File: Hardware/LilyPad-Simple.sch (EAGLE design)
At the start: 43 parts, among them U1 ATMEGA328P_TQFP, U2 MCP73831, U3 MIC5219 3.3V, Y1 8MHZ

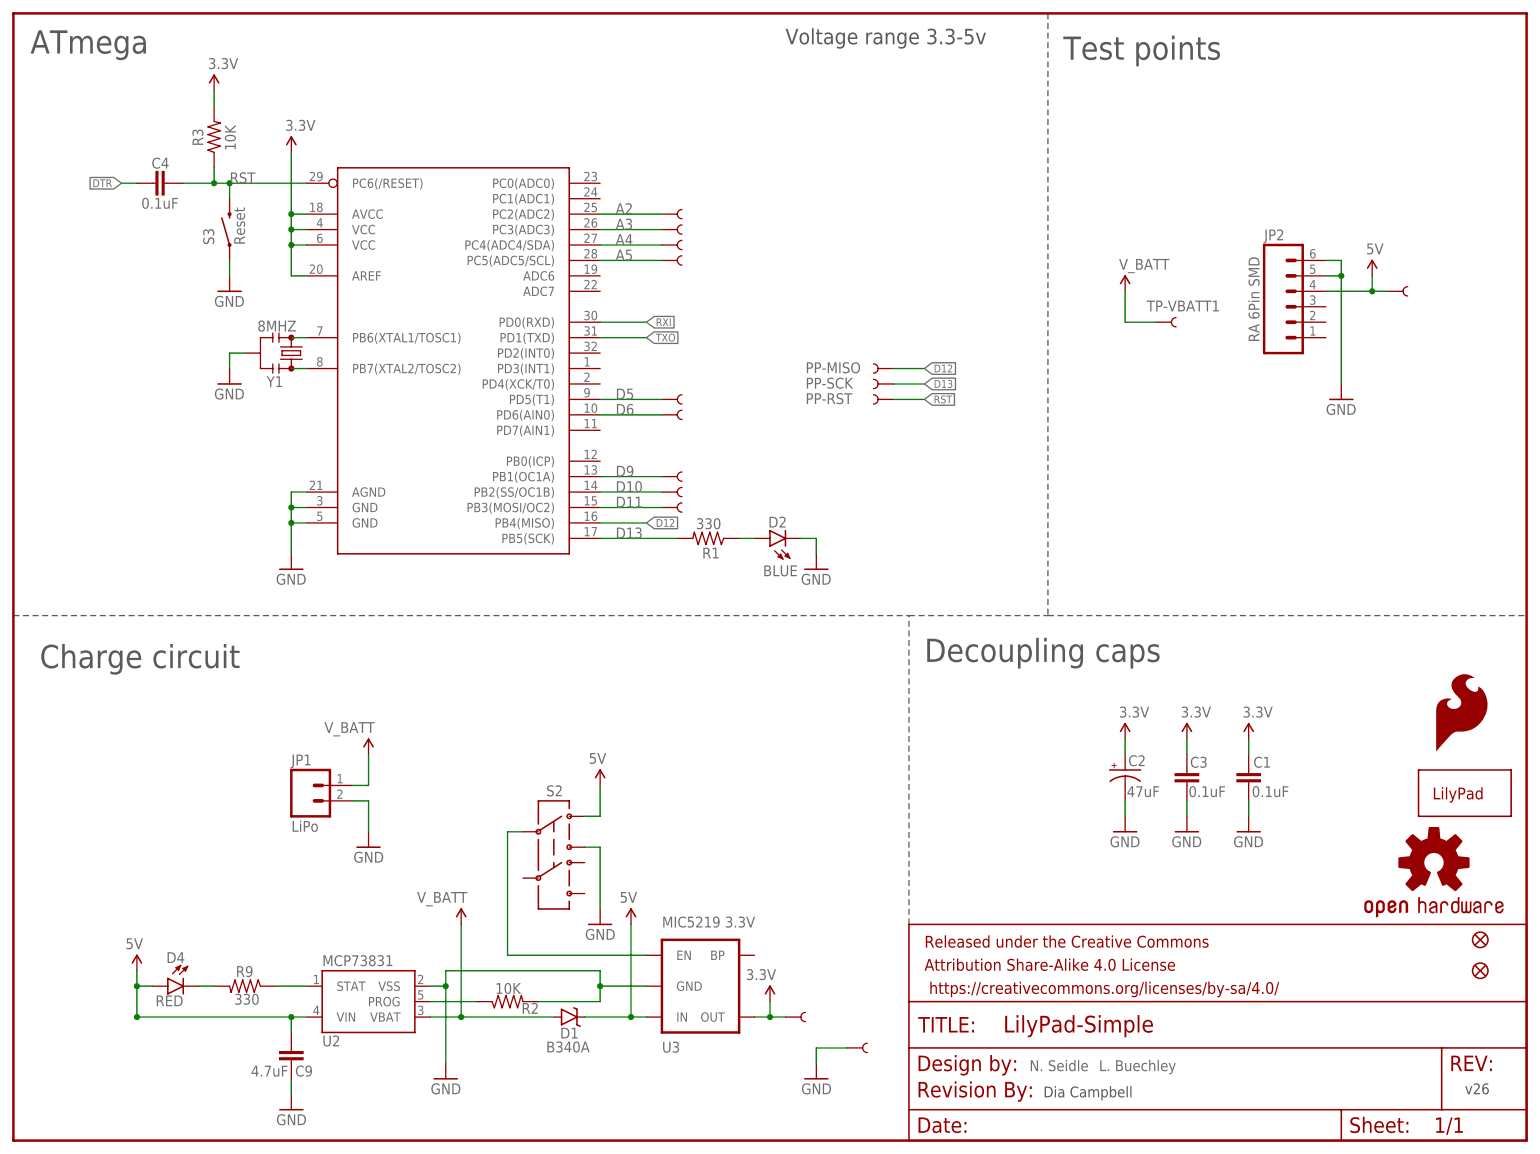
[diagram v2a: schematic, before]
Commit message: Checklist edits
Silk edited, TX and RX reconnected
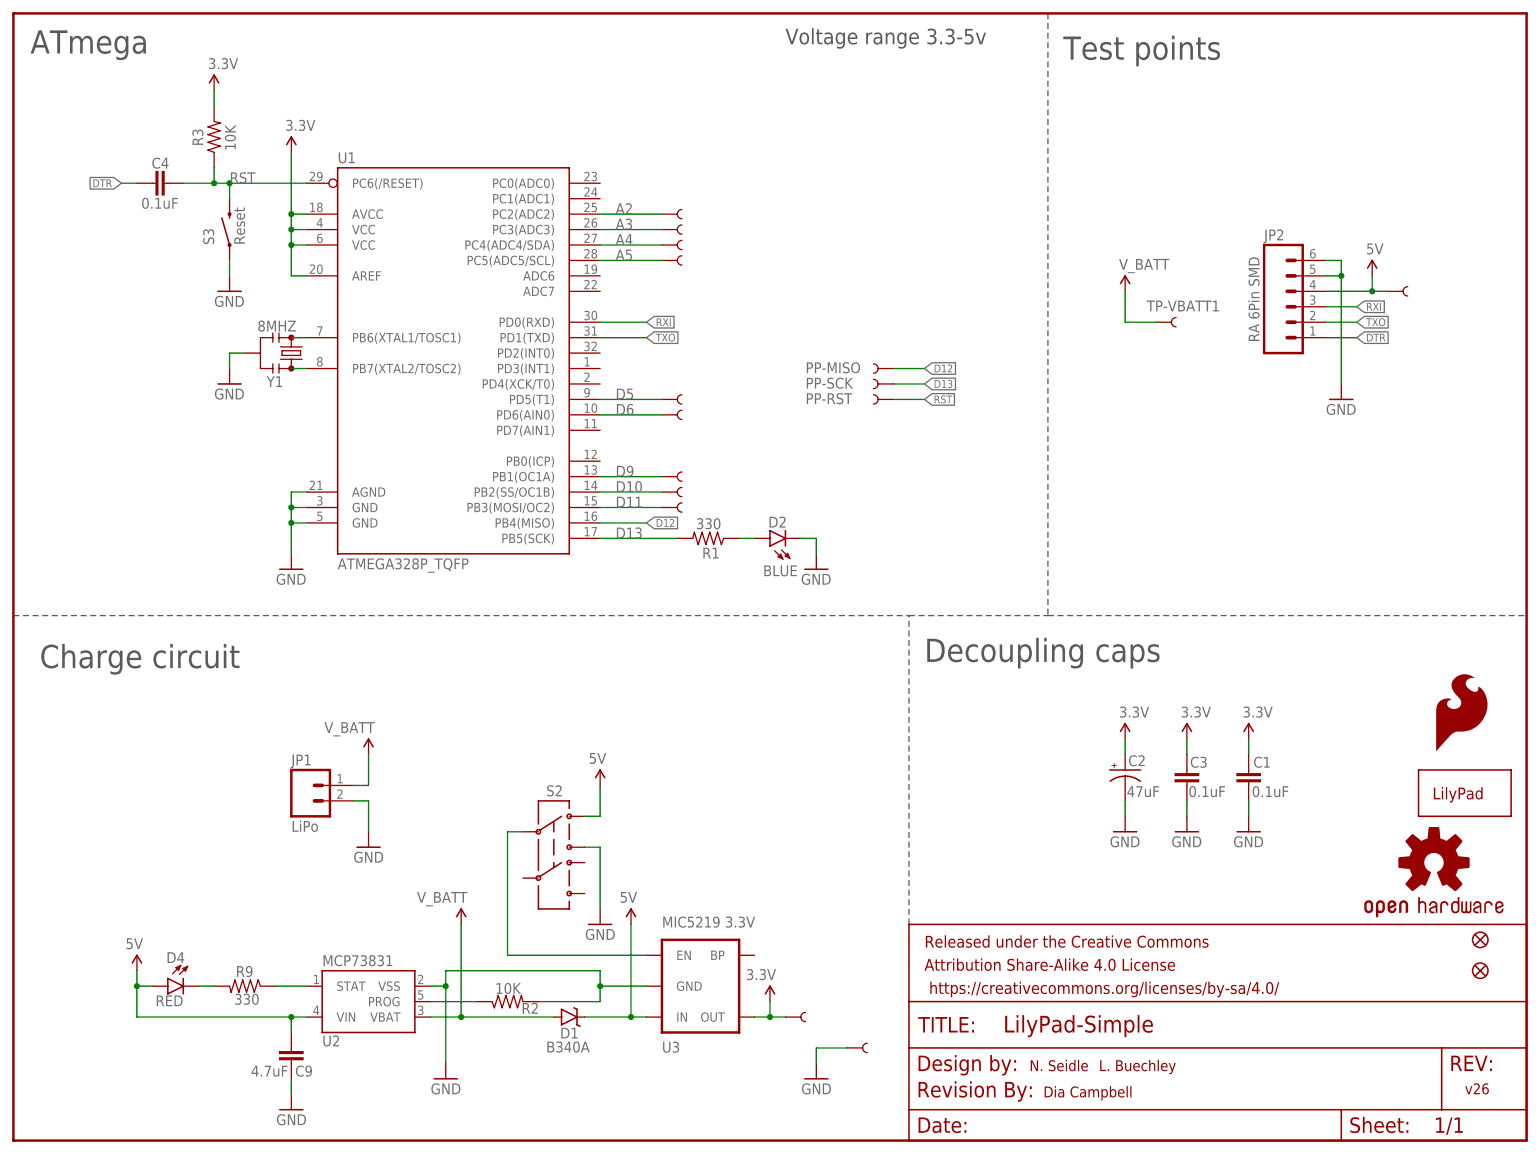
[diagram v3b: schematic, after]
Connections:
- net DTR: now also JP2.1
- net RXI: now also JP2.3
- net TXO: now also JP2.2
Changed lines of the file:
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@@
 <?xml version="1.0" encoding="utf-8"?>
 <!DOCTYPE eagle SYSTEM "eagle.dtd">
-<eagle version="7.2.0">
+<eagle version="7.3.0">
 <drawing>
 <settings>
@@
 <sheet>
 <plain>
-<text x="178.562" y="11.43" size="1.778" layer="95">L. Buechley</text>
-<text x="167.132" y="11.43" size="1.778" layer="95">N. Seidle</text>
-<text x="169.418" y="7.112" size="1.778" layer="97">Dia Campbell</text>
-<text x="238.76" y="7.62" size="1.778" layer="97">v26</text>
+<text x="178.562" y="11.43" size="1.778" layer="94">L. Buechley</text>
+<text x="167.132" y="11.43" size="1.778" layer="94">N. Seidle</text>
+<text x="169.418" y="7.112" size="1.778" layer="94">Dia Campbell</text>
+<text x="238.76" y="7.62" size="1.778" layer="94">v26</text>
 <wire x1="0" y1="86.36" x2="147.32" y2="86.36" width="0.2032" layer="97" style="longdash"/>
 <wire x1="147.32" y1="86.36" x2="170.18" y2="86.36" width="0.2032" layer="97" style="longdash"/>
@@
 <instance part="FRAME1" gate="G$1" x="0" y="0"/>
 <instance part="FRAME1" gate="V" x="147.32" y="0"/>
-<instance part="U1" gate="U$1" x="73.66" y="127" smashed="yes"/>
+<instance part="U1" gate="U$1" x="73.66" y="127" smashed="yes">
+<attribute name="NAME" x="53.34" y="160.782" size="1.778" layer="95"/>
+<attribute name="VALUE" x="53.34" y="93.98" size="1.778" layer="96"/>
+</instance>
 <instance part="A2/16" gate="G$1" x="109.22" y="152.4" smashed="yes"/>
 <instance part="A3/17" gate="G$1" x="109.22" y="149.86" smashed="yes"/>
@@
 <label x="104.14" y="134.62" size="1.27" layer="95" xref="yes"/>
 </segment>
+<segment>
+<pinref part="JP2" gate="G$1" pin="3"/>
+<wire x1="215.9" y1="137.16" x2="220.98" y2="137.16" width="0.1524" layer="91"/>
+<label x="220.98" y="137.16" size="1.27" layer="95" xref="yes"/>
+</segment>
 </net>
 <net name="TXO" class="0">
@@
 <pinref part="U1" gate="U$1" pin="PD1(TXD)"/>
 <label x="104.14" y="132.08" size="1.27" layer="95" xref="yes"/>
+</segment>
+<segment>
+<pinref part="JP2" gate="G$1" pin="2"/>
+<wire x1="215.9" y1="134.62" x2="220.98" y2="134.62" width="0.1524" layer="91"/>
+<label x="220.98" y="134.62" size="1.27" layer="95" xref="yes"/>
 </segment>
 </net>
@@
 <pinref part="C4" gate="G$1" pin="1"/>
 <label x="17.78" y="157.48" size="1.27" layer="95" rot="R180" xref="yes"/>
+</segment>
+<segment>
+<pinref part="JP2" gate="G$1" pin="1"/>
+<wire x1="215.9" y1="132.08" x2="220.98" y2="132.08" width="0.1524" layer="91"/>
+<label x="220.98" y="132.08" size="1.27" layer="95" xref="yes"/>
 </segment>
 </net>
@@
 <wire x1="22.86" y1="25.4" x2="20.32" y2="25.4" width="0.1524" layer="91"/>
 <junction x="45.72" y="20.32"/>
-<junction x="20.32" y="20.32"/>
 <pinref part="U2" gate="G$1" pin="VIN"/>
 <pinref part="C9" gate="G$1" pin="1"/>
